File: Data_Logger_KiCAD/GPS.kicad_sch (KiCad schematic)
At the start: 6 parts, among them U4 MAX-M10S

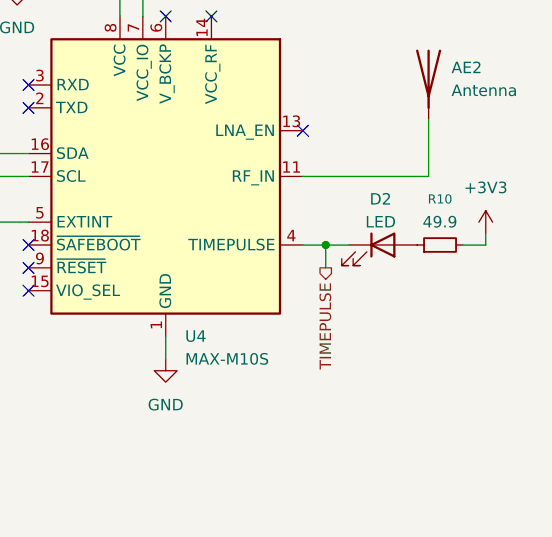
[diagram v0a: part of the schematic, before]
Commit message: rem old files and add LCSC #'s
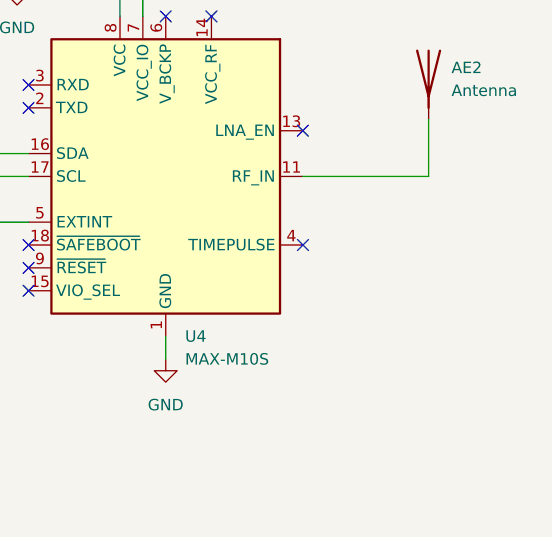
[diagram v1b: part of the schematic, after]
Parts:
- removed D2: LED, LED_SMD:LED_0603_1608Metric, symbol Device:LED
- removed R10: 49.9, Resistor_SMD:R_0402_1005Metric, symbol Device:R_Small
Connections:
- net TIMEPULSE: no longer names the net of U4.4 (TIMEPULSE)
- no-connect marks 8 -> 9

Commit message: partial MCU layout
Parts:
- AE2: footprint (none) -> custom:YG0043AA
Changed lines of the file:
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@@
 			)
 		)
-		(property "Footprint" ""
+		(property "Footprint" "custom:YG0043AA"
 			(at 151.13 64.77 0)
 			(effects

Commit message: more MCU layout
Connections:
- net +3.3V renamed +3V3
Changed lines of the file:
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@@
 			)
 		)
-		(property "Value" "+3.3V"
+		(property "Value" "+3V3"
 			(at 116.84 36.83 0)
 			(effects

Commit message: schem updates
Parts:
- added FL2: ~, custom:Filter_SAFEA1GXXKA0F00, symbol custom:SAFEA1G58KA0F00
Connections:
- net GND: now also FL2.2 (GND), FL2.3 (GND), FL2.5 (GND)
- net at AE2.1 (A): now also FL2.1 (IN); no longer U4.11 (RF_IN)
- new net: FL2.4 (OUT), U4.11 (RF_IN)
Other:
- moved on the sheet: AE2
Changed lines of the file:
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@@
+	(wire
+		(pts
+			(xy 151.13 53.34) (xy 151.13 57.15)
+		)
+		(stroke
+			(width 0)
+			(type default)
+			(color 255 0 159 1)
+		)
+	)
 	(wire
 		(pts
@@
 	(wire
 		(pts
-			(xy 151.13 76.2) (xy 151.13 69.85)
+			(xy 161.29 64.77) (xy 161.29 67.31)
+		)
+		(stroke
+			(width 0)
+			(type default)
+		)
+	)
+	(wire
+		(pts
+			(xy 158.75 64.77) (xy 161.29 64.77)
+		)
+		(stroke
+			(width 0)
+			(type default)
+		)
+	)
+	(wire
+		(pts
+			(xy 121.92 93.98) (xy 121.92 96.52)
+		)
+		(stroke
+			(width 0)
+			(type default)
+		)
+	)
+	(wire
+		(pts
+			(xy 95.25 44.45) (xy 105.41 44.45)
+		)
+		(stroke
+			(width 0)
+			(type default)
+		)
+	)
+	(wire
+		(pts
+			(xy 151.13 72.39) (xy 151.13 76.2)
 		)
 		(stroke
@@
 			(type default)
 			(color 255 0 159 1)
-		)
-	)
-	(wire
-		(pts
-			(xy 121.92 93.98) (xy 121.92 96.52)
-		)
-		(stroke
-			(width 0)
-			(type default)
-		)
-	)
-	(wire
-		(pts
-			(xy 95.25 44.45) (xy 105.41 44.45)
-		)
-		(stroke
-			(width 0)
-			(type default)
 		)
 	)
@@
 		(property "Component Class" ""
 			(at 60.96 7.62 0)
+			(effects
+				(font
+					(size 1.27 1.27)
+					(italic yes)
+				)
+			)
+		)
+	)
+	(netclass_flag ""
+		(length 2.54)
+		(shape round)
+		(at 151.13 55.88 90)
+		(fields_autoplaced yes)
+		(effects
+			(font
+				(size 1.27 1.27)
+			)
+			(justify left bottom)
+		)
+		(property "Netclass" "RF_50_SE"
+			(at 148.59 55.1815 90)
+			(effects
+				(font
+					(size 1.27 1.27)
+				)
+				(justify left)
+			)
+		)
+		(property "Component Class" ""
+			(at 72.39 -12.7 0)
 			(effects
 				(font
@@
 	(symbol
 		(lib_id "Device:Antenna")
-		(at 151.13 64.77 0)
+		(at 151.13 48.26 0)
 		(unit 1)
 		(exclude_from_sim no)
@@
 		(fields_autoplaced yes)
 		(property "Reference" "AE2"
-			(at 153.67 64.1349 0)
+			(at 153.67 47.6249 0)
 			(effects
 				(font
@@
 		)
 		(property "Value" "Antenna"
-			(at 153.67 66.6749 0)
+			(at 153.67 50.1649 0)
 			(effects
 				(font
@@
 		)
 		(property "Footprint" "custom:YG0043AA"
-			(at 151.13 64.77 0)
+			(at 151.13 48.26 0)
 			(effects
 				(font
@@
 		)
 		(property "Datasheet" "~"
-			(at 151.13 64.77 0)
+			(at 151.13 48.26 0)
 			(effects
 				(font
@@
 		)
 		(property "Description" "Antenna"
-			(at 151.13 64.77 0)
+			(at 151.13 48.26 0)
 			(effects
 				(font
@@
 	(symbol
 		(lib_id "power:GND")
+		(at 161.29 67.31 0)
+		(unit 1)
+		(exclude_from_sim no)
+		(in_bom yes)
+		(on_board yes)
+		(dnp no)
+		(fields_autoplaced yes)
+		(property "Reference" "#PWR021"
+			(at 161.29 73.66 0)
+			(effects
+				(font
+					(size 1.27 1.27)
+				)
+				(hide yes)
+			)
+		)
+		(property "Value" "GND"
+			(at 161.29 72.39 0)
+			(effects
+				(font
+					(size 1.27 1.27)
+				)
+			)
+		)
+		(property "Footprint" ""
+			(at 161.29 67.31 0)
+			(effects
+				(font
+					(size 1.27 1.27)
+				)
+				(hide yes)
+			)
+		)
+		(property "Datasheet" ""
+			(at 161.29 67.31 0)
+			(effects
+				(font
+					(size 1.27 1.27)
+				)
+				(hide yes)
+			)
+		)
+		(property "Description" "Power symbol creates a global label with name \"GND\" , ground"
+			(at 161.29 67.31 0)
+			(effects
+				(font
+					(size 1.27 1.27)
+				)
+				(hide yes)
+			)
+		)
+		(pin "1"
+		)
+		(instances
+			(project "Data_Logger_Board"
+				(path "/db968e42-3ace-4cc9-9096-9d8f48135c40/795ab2be-9db7-4254-b05c-ac2b60177344/bd56c2d0-6430-41ab-a92d-256e41365a97"
+					(reference "#PWR021")
+					(unit 1)
+				)
+			)
+		)
+	)
+	(symbol
+		(lib_id "power:GND")
 		(at 95.25 54.61 0)
 		(unit 1)
@@
 					(unit 1)
 				)
+			)
+		)
+	)
+	(symbol
+		(lib_id "custom:SAFEA1G58KA0F00")
+		(at 151.13 64.77 90)
+		(mirror x)
+		(unit 1)
+		(exclude_from_sim no)
+		(in_bom yes)
+		(on_board yes)
+		(dnp no)
+		(fields_autoplaced yes)
+		(property "Reference" "FL2"
+			(at 144.78 64.1349 90)
+			(effects
+				(font
+					(size 1.27 1.27)
+				)
+				(justify left)
+			)
+		)
+		(property "Value" "~"
+			(at 144.78 66.04 90)
+			(effects
+				(font
+					(size 1.27 1.27)
+				)
+				(justify left)
+			)
+		)
+		(property "Footprint" "custom:Filter_SAFEA1GXXKA0F00"
+			(at 151.13 64.77 0)
+			(effects
+				(font
+					(size 1.27 1.27)
+				)
+				(hide yes)
+			)
+		)
+		(property "Datasheet" ""
+			(at 151.13 64.77 0)
+			(effects
+				(font
+					(size 1.27 1.27)
+				)
+				(hide yes)
+			)
+		)
+		(property "Description" ""
+			(at 151.13 64.77 0)
+			(effects
+				(font
+					(size 1.27 1.27)
+				)
+				(hide yes)
+			)
+		)
+		(property "LCSC" "C91641"
+			(at 151.13 64.77 90)
+			(effects
+				(font
+					(size 1.27 1.27)
+				)
+				(hide yes)
+			)
+		)
+		(pin "5"
+		)
+		(pin "3"
+		)
+		(pin "2"
+		)
+		(pin "1"
+		)
+		(pin "4"
+		)
+		(instances
+			(project "Data_Logger_Board"
+				(path "/db968e42-3ace-4cc9-9096-9d8f48135c40/795ab2be-9db7-4254-b05c-ac2b60177344/bd56c2d0-6430-41ab-a92d-256e41365a97"
+					(reference "FL2")
+					(unit 1)
+				)

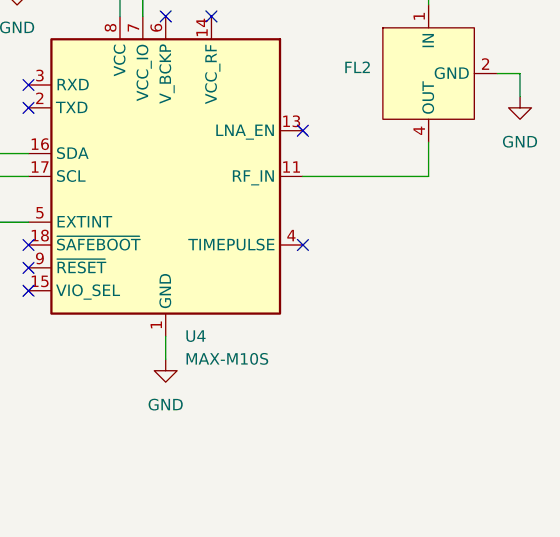
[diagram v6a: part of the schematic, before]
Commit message: layout
fix rf, usb netclass, add timepulse, round dimensions to even number, re-route GPS, 22 ohm in usb line, buttons to front, reg to front, change solder jumper for conn
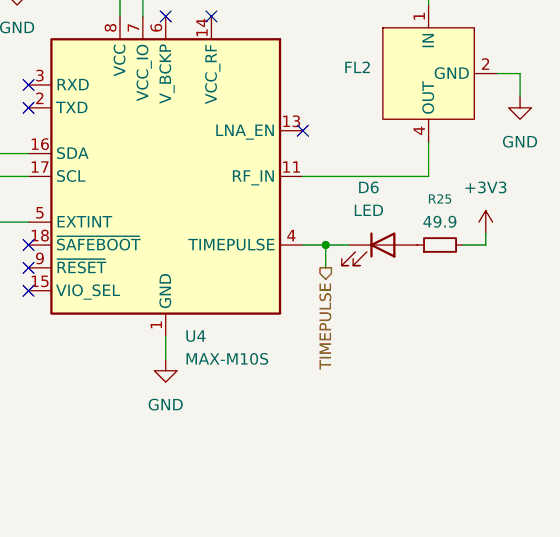
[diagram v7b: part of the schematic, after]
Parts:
- added D6: LED, LED_SMD:LED_0603_1608Metric, symbol Device:LED
- added R25: 49.9, Resistor_SMD:R_0402_1005Metric, symbol Device:R_Small
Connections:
- net +3V3: now also R25.2
- net TIMEPULSE: now reaches U4.4 (TIMEPULSE)
- net TIMEPULSE: now also D6.1 (K)
- new net: D6.2 (A), R25.1
- no-connect marks 9 -> 8

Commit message: schematic recs
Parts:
- D6: value LED -> Amber
- R25: value 49.9 -> 1k; LCSC C25120 -> C11702
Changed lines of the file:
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@@
 			)
 		)
-		(property "Value" "49.9"
+		(property "Value" "1k"
 			(at 152.4 81.28 90)
 			(effects
@@
 			)
 		)
-		(property "LCSC" "C25120"
+		(property "LCSC" "C11702"
 			(at 152.4 83.82 0)
 			(effects
@@
 			)
 		)
-		(property "Value" "LED"
+		(property "Value" "Amber"
 			(at 144.4625 80.01 0)
 			(effects
